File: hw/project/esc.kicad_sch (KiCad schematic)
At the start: 0 parts

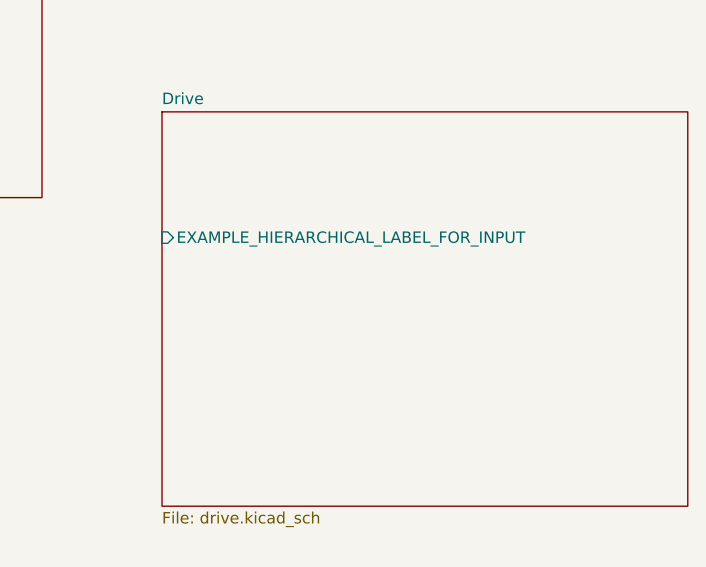
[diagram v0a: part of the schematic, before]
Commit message: Set up Drive schem
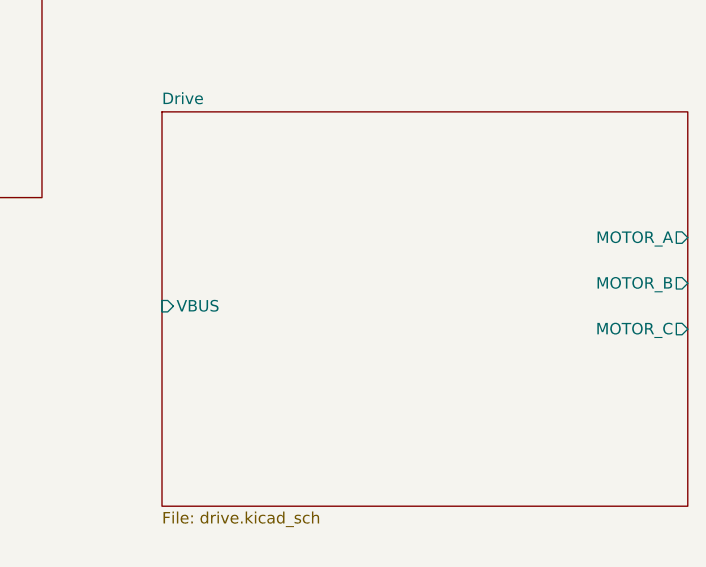
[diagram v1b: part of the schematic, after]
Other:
- sheet Drive ports: added MOTOR_A, MOTOR_B, MOTOR_C, VBUS; removed EXAMPLE_HIERARCHICAL_LABEL_FOR_INPUT
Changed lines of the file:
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@@
 			)
 		)
-		(pin "EXAMPLE_HIERARCHICAL_LABEL_FOR_INPUT" input
-			(at 120.015 101.6 180)
+		(pin "MOTOR_A" output
+			(at 178.435 101.6 0)
 			(effects
 				(font
+					(size 1.27 1.27)
+				)
+				(justify right)
+			)
+		)
+		(pin "MOTOR_B" output
+			(at 178.435 106.68 0)
+			(effects
+				(font
+					(size 1.27 1.27)
+				)
+				(justify right)
+			)
+		)
+		(pin "MOTOR_C" output
+			(at 178.435 111.76 0)
+			(effects
+				(font
+					(size 1.27 1.27)
+				)
+				(justify right)
+			)
+		)
+		(pin "VBUS" input
+			(at 120.015 109.22 180)
+			(effects
+				(font

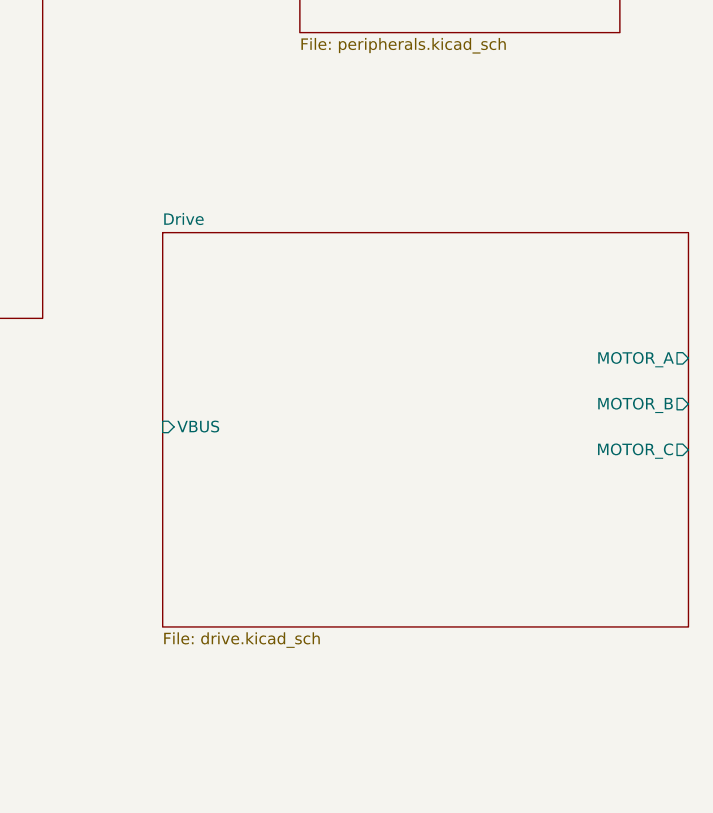
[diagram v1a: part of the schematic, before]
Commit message: Done with Drive stage EXCEPT analog sensing
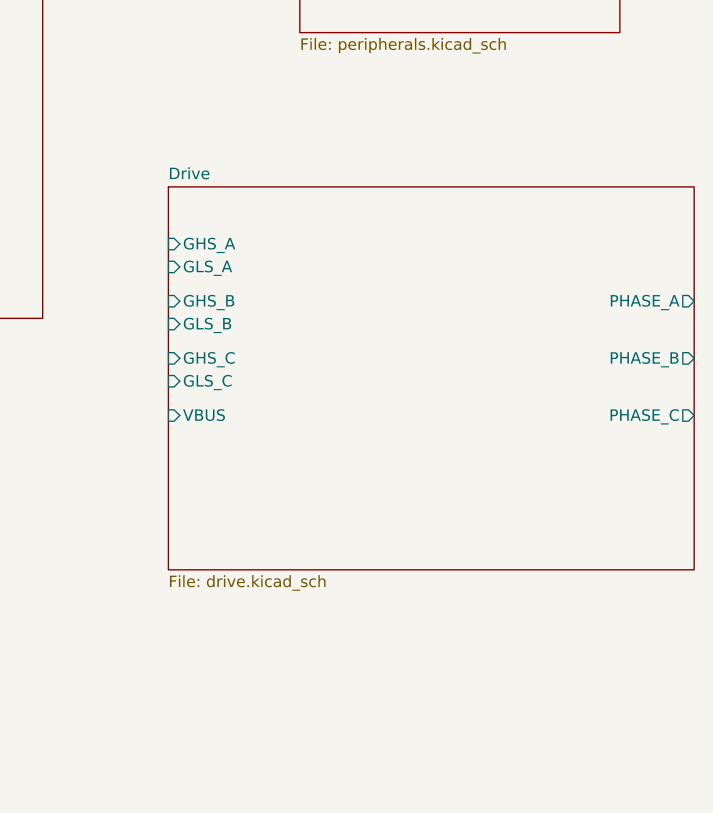
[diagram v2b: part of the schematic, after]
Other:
- sheet Drive ports: added GHS_A, GHS_B, GHS_C, GLS_A, GLS_B, GLS_C, PHASE_A, PHASE_B, PHASE_C; removed MOTOR_A, MOTOR_B, MOTOR_C
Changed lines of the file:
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@@
 	)
 	(sheet
-		(at 120.015 87.63)
-		(size 58.42 43.815)
+		(at 120.65 82.55)
+		(size 58.42 42.545)
 		(exclude_from_sim no)
 		(in_bom yes)
@@
 		)
 		(property "Sheetname" "Drive"
-			(at 120.015 86.9184 0)
+			(at 120.65 81.8384 0)
 			(effects
 				(font
@@
 		)
 		(property "Sheetfile" "drive.kicad_sch"
-			(at 120.015 132.0296 0)
+			(at 120.65 125.6796 0)
 			(effects
 				(font
@@
 			)
 		)
-		(pin "MOTOR_A" output
-			(at 178.435 101.6 0)
+		(pin "VBUS" input
+			(at 120.65 107.95 180)
+			(effects
+				(font
+					(size 1.27 1.27)
+				)
+				(justify left)
+			)
+		)
+		(pin "GHS_C" input
+			(at 120.65 101.6 180)
+			(effects
+				(font
+					(size 1.27 1.27)
+				)
+				(justify left)
+			)
+		)
+		(pin "PHASE_C" output
+			(at 179.07 107.95 0)
 			(effects
 				(font
@@
 			)
 		)
-		(pin "MOTOR_B" output
-			(at 178.435 106.68 0)
+		(pin "GHS_A" input
+			(at 120.65 88.9 180)
+			(effects
+				(font
+					(size 1.27 1.27)
+				)
+				(justify left)
+			)
+		)
+		(pin "GLS_A" input
+			(at 120.65 91.44 180)
+			(effects
+				(font
+					(size 1.27 1.27)
+				)
+				(justify left)
+			)
+		)
+		(pin "PHASE_B" output
+			(at 179.07 101.6 0)
 			(effects
 				(font
@@
 			)
 		)
-		(pin "MOTOR_C" output
-			(at 178.435 111.76 0)
+		(pin "PHASE_A" output
+			(at 179.07 95.25 0)
 			(effects
 				(font
@@
 			)
 		)
-		(pin "VBUS" input
-			(at 120.015 109.22 180)
+		(pin "GLS_C" input
+			(at 120.65 104.14 180)
 			(effects
 				(font
+					(size 1.27 1.27)
+				)
+				(justify left)
+			)
+		)
+		(pin "GHS_B" input
+			(at 120.65 95.25 180)
+			(effects
+				(font
+					(size 1.27 1.27)
+				)
+				(justify left)
+			)
+		)
+		(pin "GLS_B" input
+			(at 120.65 97.79 180)
+			(effects
+				(font

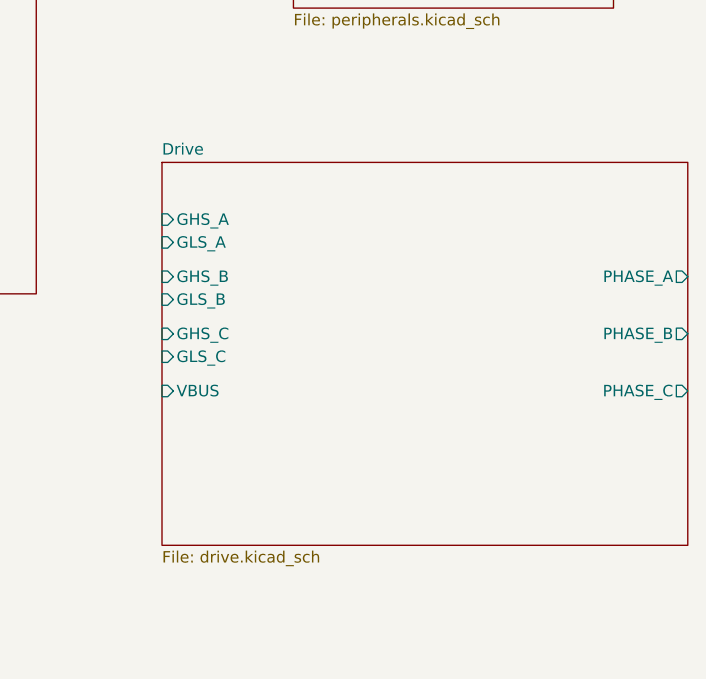
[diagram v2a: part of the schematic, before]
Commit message: Added STM to Control sheet and proj libs
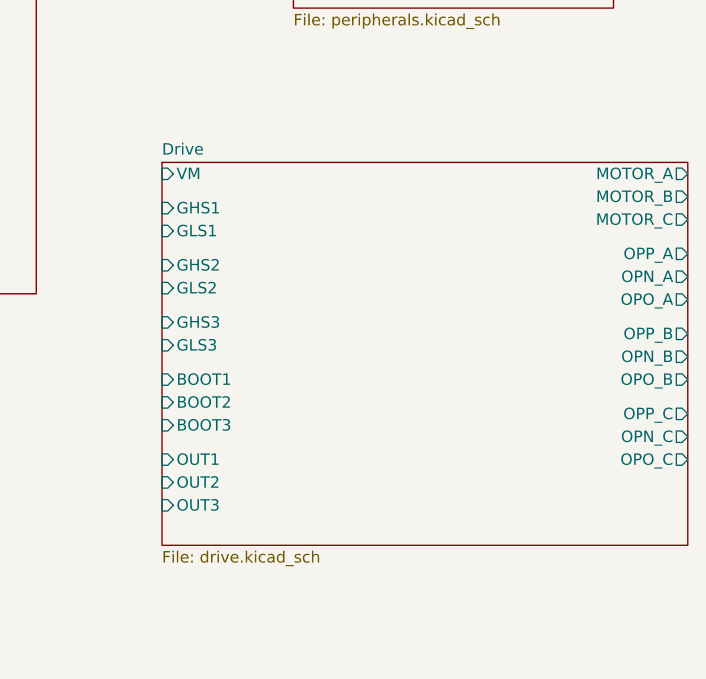
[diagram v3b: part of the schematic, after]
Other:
- sheet Drive ports: added BOOT1, BOOT2, BOOT3, GHS1, GHS2, GHS3, GLS1, GLS2, GLS3, MOTOR_A, MOTOR_B, MOTOR_C, OPN_A, OPN_B, OPN_C, OPO_A, OPO_B, OPO_C, OPP_A, OPP_B, OPP_C, OUT1, OUT2, OUT3, VM; removed GHS_A, GHS_B, GHS_C, GLS_A, GLS_B, GLS_C, PHASE_A, PHASE_B, PHASE_C, VBUS
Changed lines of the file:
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@@
 			)
 		)
-		(pin "VBUS" input
-			(at 120.65 107.95 180)
-			(effects
-				(font
-					(size 1.27 1.27)
-				)
-				(justify left)
-			)
-		)
-		(pin "GHS_C" input
-			(at 120.65 101.6 180)
-			(effects
-				(font
-					(size 1.27 1.27)
-				)
-				(justify left)
-			)
-		)
-		(pin "PHASE_C" output
-			(at 179.07 107.95 0)
-			(effects
-				(font
-					(size 1.27 1.27)
-				)
-				(justify right)
-			)
-		)
-		(pin "GHS_A" input
-			(at 120.65 88.9 180)
-			(effects
-				(font
-					(size 1.27 1.27)
-				)
-				(justify left)
-			)
-		)
-		(pin "GLS_A" input
-			(at 120.65 91.44 180)
-			(effects
-				(font
-					(size 1.27 1.27)
-				)
-				(justify left)
-			)
-		)
-		(pin "PHASE_B" output
+		(pin "MOTOR_C" output
+			(at 179.07 88.9 0)
+			(effects
+				(font
+					(size 1.27 1.27)
+				)
+				(justify right)
+			)
+		)
+		(pin "GLS3" input
+			(at 120.65 102.87 180)
+			(effects
+				(font
+					(size 1.27 1.27)
+				)
+				(justify left)
+			)
+		)
+		(pin "GHS2" input
+			(at 120.65 93.98 180)
+			(effects
+				(font
+					(size 1.27 1.27)
+				)
+				(justify left)
+			)
+		)
+		(pin "VM" input
+			(at 120.65 83.82 180)
+			(effects
+				(font
+					(size 1.27 1.27)
+				)
+				(justify left)
+			)
+		)
+		(pin "GHS1" input
+			(at 120.65 87.63 180)
+			(effects
+				(font
+					(size 1.27 1.27)
+				)
+				(justify left)
+			)
+		)
+		(pin "GHS3" input
+			(at 120.65 100.33 180)
+			(effects
+				(font
+					(size 1.27 1.27)
+				)
+				(justify left)
+			)
+		)
+		(pin "MOTOR_A" output
+			(at 179.07 83.82 0)
+			(effects
+				(font
+					(size 1.27 1.27)
+				)
+				(justify right)
+			)
+		)
+		(pin "GLS2" input
+			(at 120.65 96.52 180)
+			(effects
+				(font
+					(size 1.27 1.27)
+				)
+				(justify left)
+			)
+		)
+		(pin "MOTOR_B" output
+			(at 179.07 86.36 0)
+			(effects
+				(font
+					(size 1.27 1.27)
+				)
+				(justify right)
+			)
+		)
+		(pin "OUT2" input
+			(at 120.65 118.11 180)
+			(effects
+				(font
+					(size 1.27 1.27)
+				)
+				(justify left)
+			)
+		)
+		(pin "BOOT3" input
+			(at 120.65 111.76 180)
+			(effects
+				(font
+					(size 1.27 1.27)
+				)
+				(justify left)
+			)
+		)
+		(pin "OUT1" input
+			(at 120.65 115.57 180)
+			(effects
+				(font
+					(size 1.27 1.27)
+				)
+				(justify left)
+			)
+		)
+		(pin "BOOT1" input
+			(at 120.65 106.68 180)
+			(effects
+				(font
+					(size 1.27 1.27)
+				)
+				(justify left)
+			)
+		)
+		(pin "OUT3" input
+			(at 120.65 120.65 180)
+			(effects
+				(font
+					(size 1.27 1.27)
+				)
+				(justify left)
+			)
+		)
+		(pin "BOOT2" input
+			(at 120.65 109.22 180)
+			(effects
+				(font
+					(size 1.27 1.27)
+				)
+				(justify left)
+			)
+		)
+		(pin "GLS1" input
+			(at 120.65 90.17 180)
+			(effects
+				(font
+					(size 1.27 1.27)
+				)
+				(justify left)
+			)
+		)
+		(pin "OPN_A" output
+			(at 179.07 95.25 0)
+			(effects
+				(font
+					(size 1.27 1.27)
+				)
+				(justify right)
+			)
+		)
+		(pin "OPO_A" output
+			(at 179.07 97.79 0)
+			(effects
+				(font
+					(size 1.27 1.27)
+				)
+				(justify right)
+			)
+		)
+		(pin "OPO_B" output
+			(at 179.07 106.68 0)
+			(effects
+				(font
+					(size 1.27 1.27)
+				)
+				(justify right)
+			)
+		)
+		(pin "OPP_A" output
+			(at 179.07 92.71 0)
+			(effects
+				(font
+					(size 1.27 1.27)
+				)
+				(justify right)
+			)
+		)
+		(pin "OPO_C" output
+			(at 179.07 115.57 0)
+			(effects
+				(font
+					(size 1.27 1.27)
+				)
+				(justify right)
+			)
+		)
+		(pin "OPN_B" output
+			(at 179.07 104.14 0)
+			(effects
+				(font
+					(size 1.27 1.27)
+				)
+				(justify right)
+			)
+		)
+		(pin "OPP_B" output
 			(at 179.07 101.6 0)
 			(effects
@@
 			)
 		)
-		(pin "PHASE_A" output
-			(at 179.07 95.25 0)
-			(effects
-				(font
-					(size 1.27 1.27)
-				)
-				(justify right)
-			)
-		)
-		(pin "GLS_C" input
-			(at 120.65 104.14 180)
-			(effects
-				(font
-					(size 1.27 1.27)
-				)
-				(justify left)
-			)
-		)
-		(pin "GHS_B" input
-			(at 120.65 95.25 180)
-			(effects
-				(font
-					(size 1.27 1.27)
-				)
-				(justify left)
-			)
-		)
-		(pin "GLS_B" input
-			(at 120.65 97.79 180)
-			(effects
-				(font
-					(size 1.27 1.27)
-				)
-				(justify left)
-			)
-		)
+		(pin "OPN_C" output
+			(at 179.07 113.03 0)
+			(effects
+				(font
+					(size 1.27 1.27)
+				)
+				(justify right)
+			)
+		)
+		(pin "OPP_C" output
+			(at 179.07 110.49 0)
+			(effects
+				(font
+					(size 1.27 1.27)
+				)
+				(justify right)
+			)
+		)

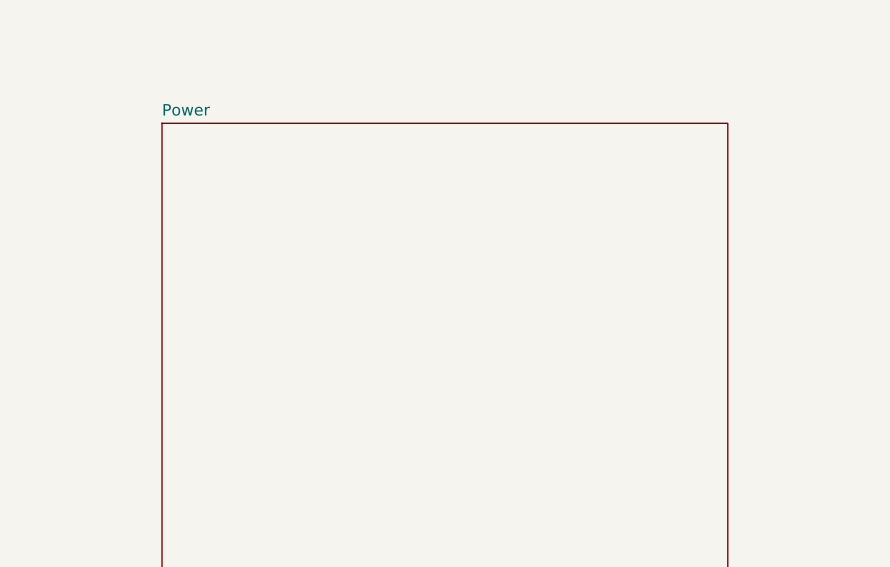
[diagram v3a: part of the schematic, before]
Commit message: Cleaned up symbols and added footprint/3d model
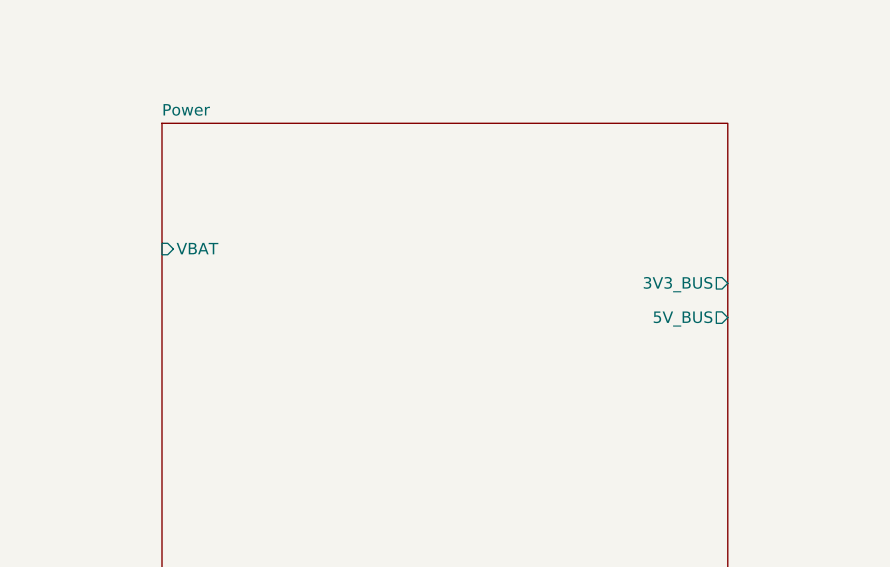
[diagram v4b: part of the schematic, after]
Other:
- sheet Power ports: added 3V3_BUS, 5V_BUS, VBAT; removed none
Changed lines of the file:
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@@
+			)
+		)
+		(pin "VBAT" input
+			(at 30.48 129.54 180)
+			(effects
+				(font
+					(size 1.27 1.27)
+				)
+				(justify left)
+			)
+		)
+		(pin "3V3_BUS" output
+			(at 93.345 133.35 0)
+			(effects
+				(font
+					(size 1.27 1.27)
+				)
+				(justify right)
+			)
+		)
+		(pin "5V_BUS" output
+			(at 93.345 137.16 0)
+			(effects
+				(font
+					(size 1.27 1.27)
+				)
+				(justify right)
 			)
 		)
